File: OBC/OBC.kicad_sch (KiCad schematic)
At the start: 10 parts, among them J101 IDC1 (PMS-Raspi), J102 Modo de operación, J103 IDC2 (Raspi-TRU), J104 Conn_01x04, U101 RASPBERRY_PI_ZERO_2_W, U102 BMP280, U103 MPU9250

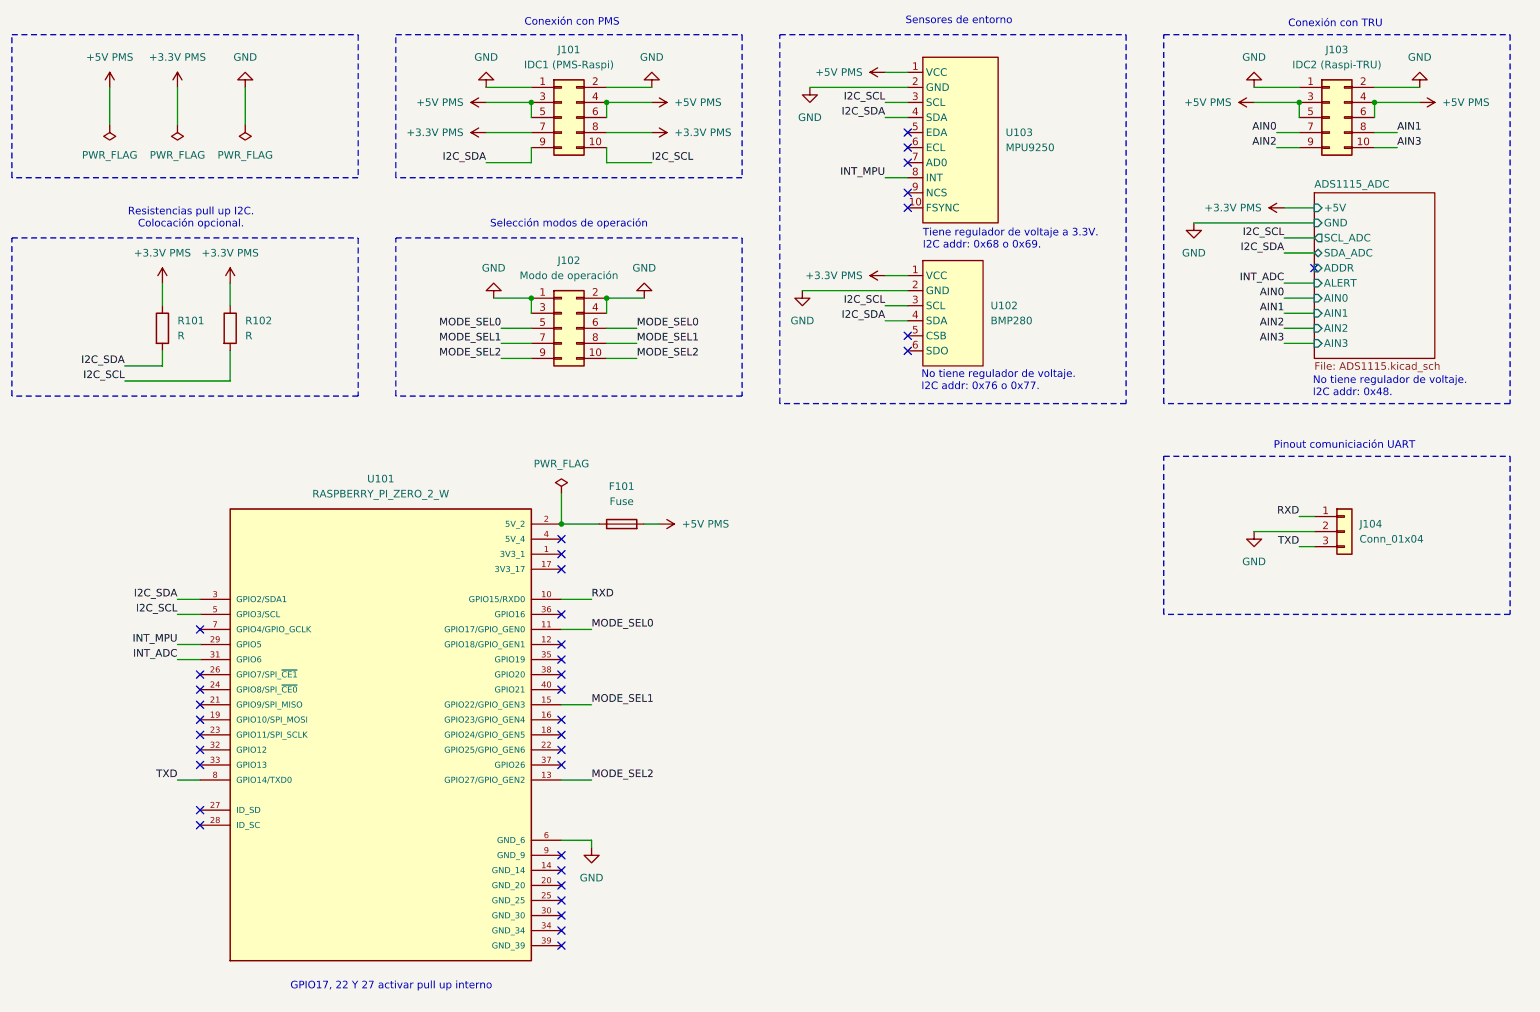
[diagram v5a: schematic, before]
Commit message: Cambia conectores IDC por JST
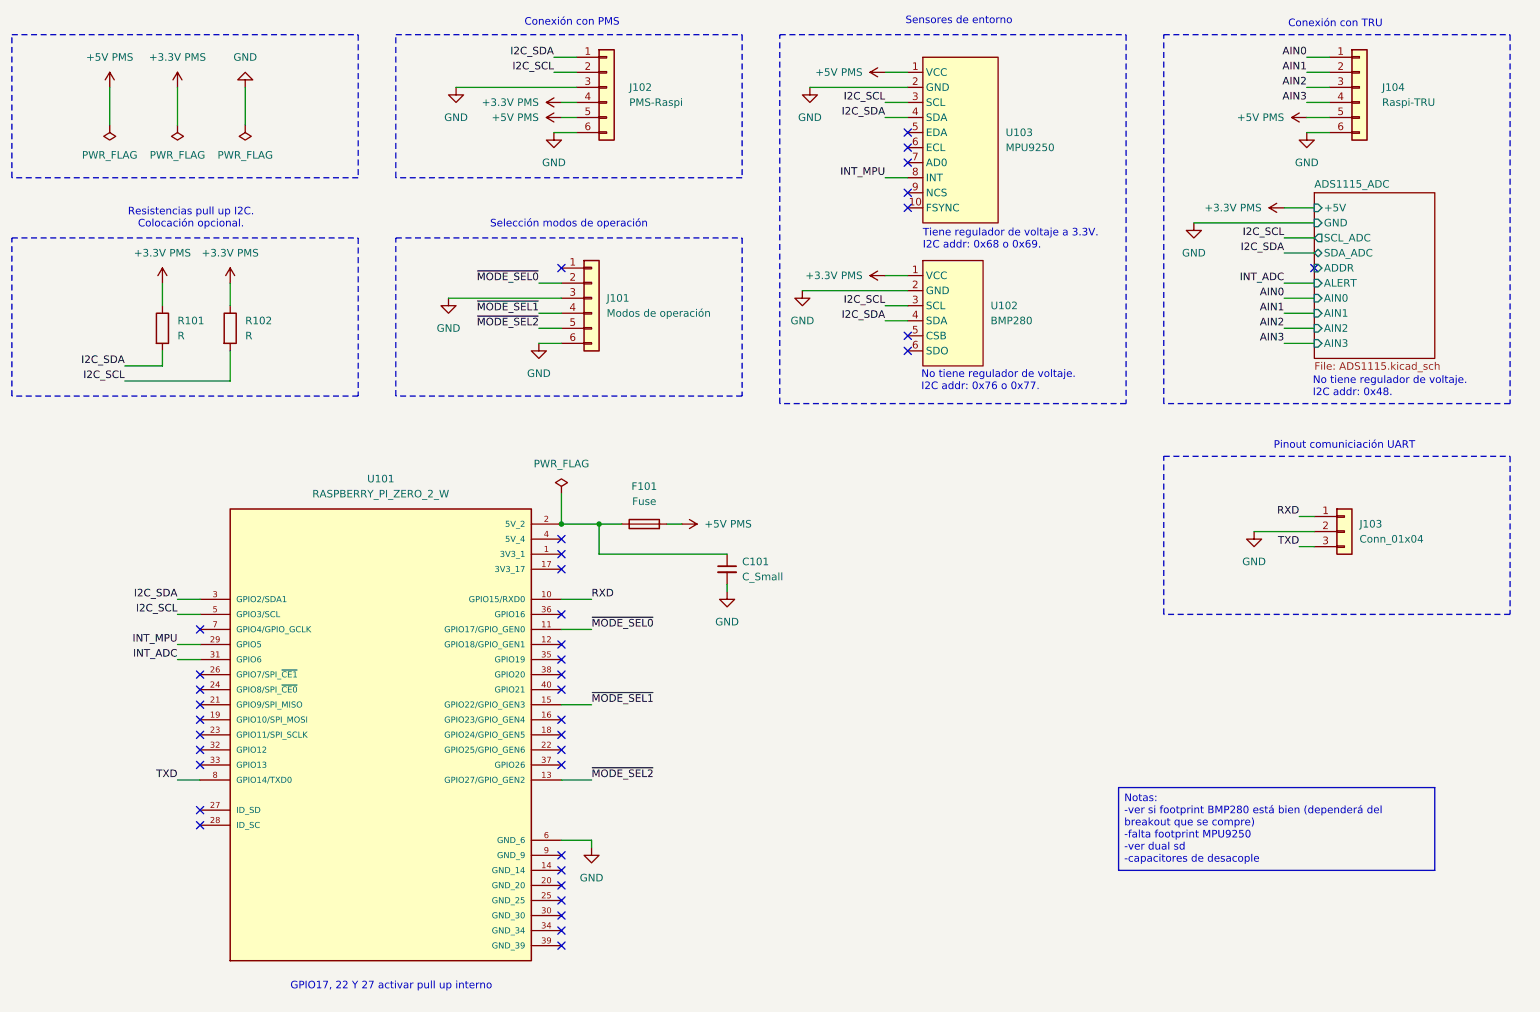
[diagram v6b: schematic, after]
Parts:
- removed J101: IDC1 (PMS-Raspi), symbol Connector_Generic:Conn_02x05_Odd_Even
- removed J102: Modo de operación, symbol Connector_Generic:Conn_02x05_Odd_Even
- removed J103: IDC2 (Raspi-TRU), symbol Connector_Generic:Conn_02x05_Odd_Even
- added C101: C_Small, symbol Device:C_Small
- added J101: Modos de operación, symbol Connector_Generic:Conn_01x06
- added J102: PMS-Raspi, symbol Connector_Generic:Conn_01x06
- added J104: Raspi-TRU, symbol Connector_Generic:Conn_01x06
- renumbered J104 to J103
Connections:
- net +3.3V PMS: now also J102.4 (Pin_4)
- net +5V PMS: now also J102.5 (Pin_5), J104.5 (Pin_5)
- net AIN0: now also J104.1 (Pin_1)
- net AIN1: now also J104.2 (Pin_2)
- net AIN2: now also J104.3 (Pin_3)
- net AIN3: now also J104.4 (Pin_4)
- net GND: now also C101.2, J101.3 (Pin_3), J101.6 (Pin_6), J102.3 (Pin_3), J102.6 (Pin_6), J104.6 (Pin_6)
- net I2C_SCL: now also J102.2 (Pin_2)
- net I2C_SDA: now also J102.1 (Pin_1)
- net at F101.1, U101.2 (5V_2): now also C101.1
- net MODE_SEL0 renamed ~{MODE_SEL0}
- net ~{MODE_SEL0}: now also J101.2 (Pin_2)
- net MODE_SEL1 renamed ~{MODE_SEL1}
- net ~{MODE_SEL1}: now also J101.4 (Pin_4)
- net MODE_SEL2 renamed ~{MODE_SEL2}
- net ~{MODE_SEL2}: now also J101.5 (Pin_5)
- no-connect marks 37 -> 38
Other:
- moved on the sheet: F101

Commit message: Agrega resistencias en serie con NTC
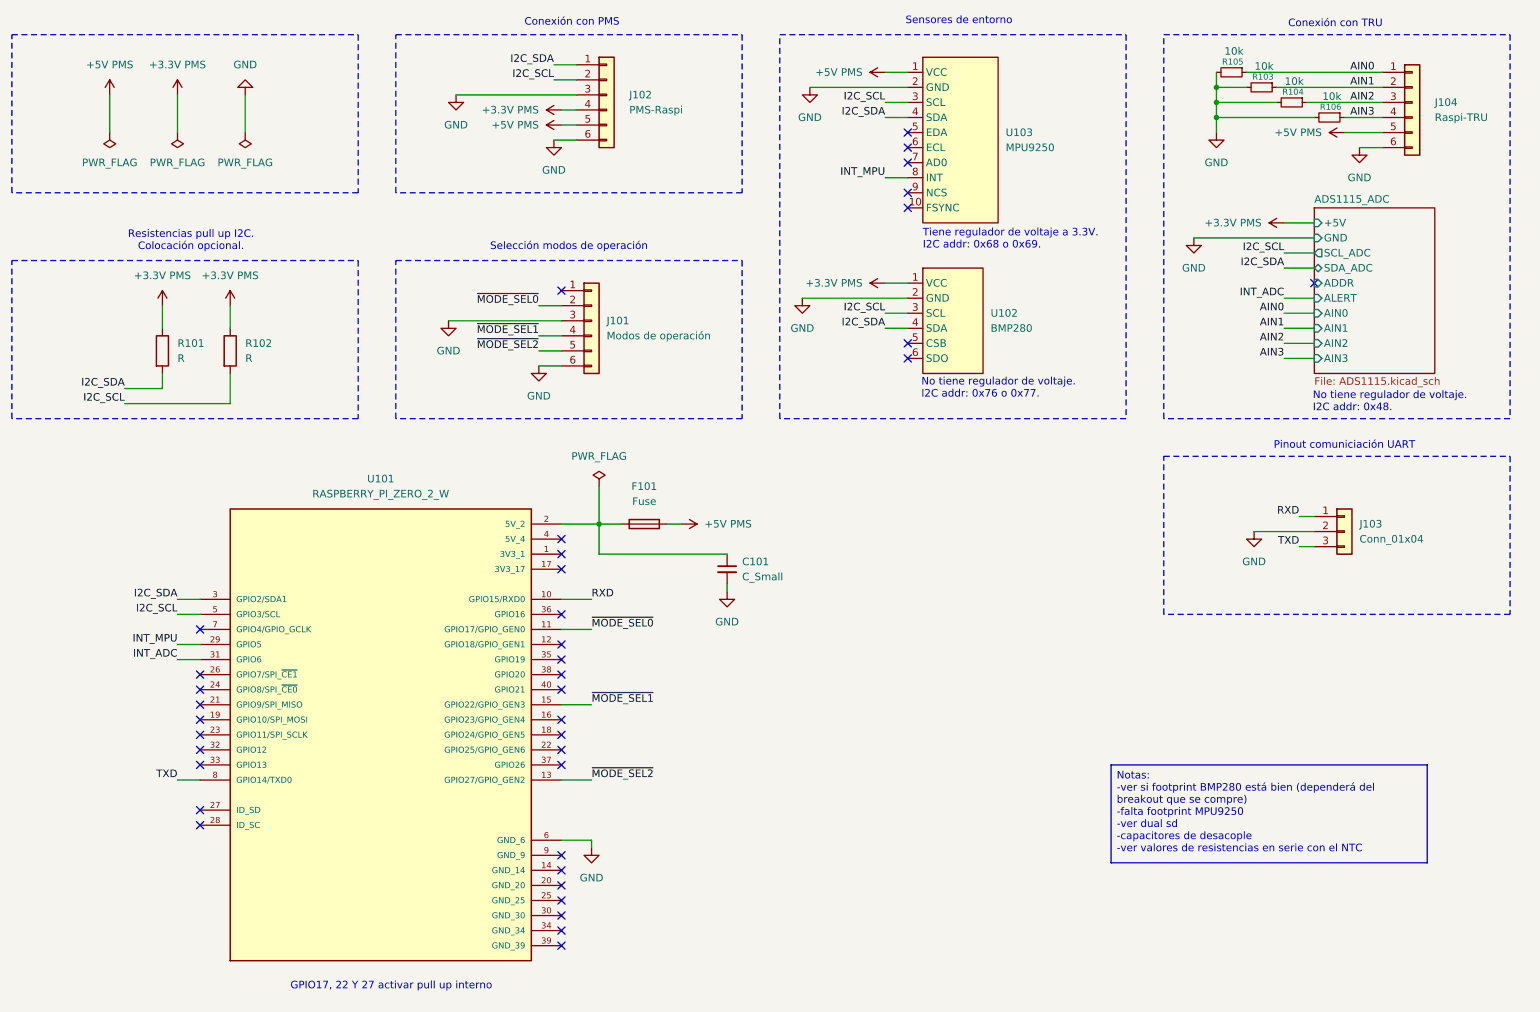
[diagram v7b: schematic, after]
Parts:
- added R103, R104, R105, R106: 10k, symbol Device:R_Small
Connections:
- net AIN0: now also R105.1
- net AIN1: now also R103.1
- net AIN2: now also R104.1
- net AIN3: now also R106.1
- net GND: now also R103.2, R104.2, R105.2, R106.2
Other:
- moved on the sheet: J101, J102, J104, R101, R102, U102

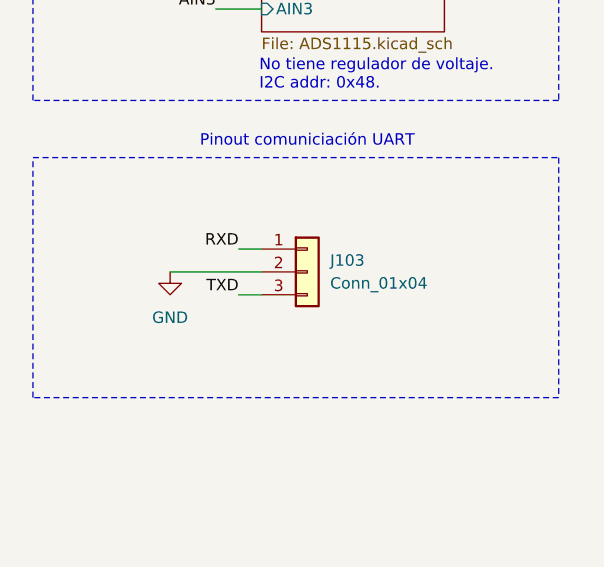
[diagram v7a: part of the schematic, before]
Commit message: Empieza con pcb
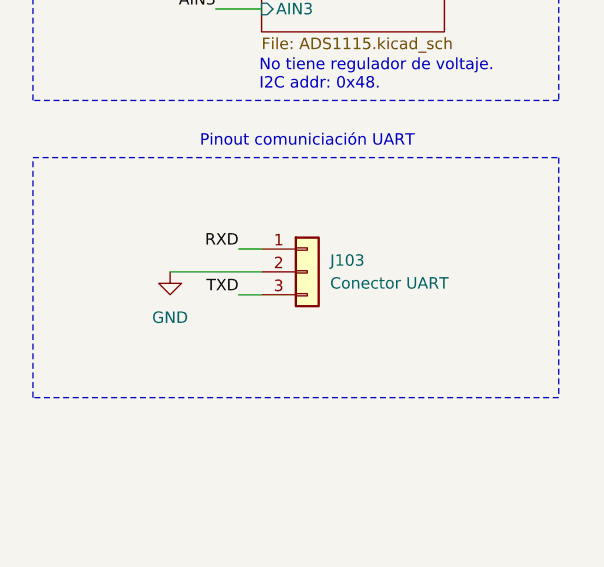
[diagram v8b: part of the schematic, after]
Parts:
- C101: footprint (none) -> Capacitor_SMD:C_0402_1005Metric
- F101: footprint (none) -> Fuse:Fuse_BelFuse_0ZRE0005FF_L8.3mm_W3.8mm
- J101, J102, J104: footprint (none) -> Connector_JST:JST_XH_S6B-XH-A_1x06_P2.50mm_Horizontal
- J103: value Conn_01x04 -> Conector UART; footprint (none) -> Connector_JST:JST_XH_S3B-XH-A-1_1x03_P2.50mm_Horizontal
- R101, R102, R103, R104, R105, R106: footprint (none) -> Resistor_SMD:R_0603_1608Metric
- U102: footprint Charleslabs_Parts:BMP280_Module -> cubesat:BMP280_Module
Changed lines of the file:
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@@
 			)
 		)
-		(property "Footprint" ""
+		(property "Footprint" "Resistor_SMD:R_0603_1608Metric"
 			(at 242.57 38.1 0)
 			(effects
@@
 			)
 		)
-		(property "Footprint" ""
+		(property "Footprint" "Connector_JST:JST_XH_S6B-XH-A_1x06_P2.50mm_Horizontal"
 			(at 120.65 34.29 0)
 			(effects
@@
 			)
 		)
-		(property "Footprint" ""
+		(property "Footprint" "Connector_JST:JST_XH_S6B-XH-A_1x06_P2.50mm_Horizontal"
 			(at 256.54 35.56 0)
 			(effects
@@
 			)
 		)
-		(property "Footprint" ""
+		(property "Footprint" "Capacitor_SMD:C_0402_1005Metric"
 			(at 140.97 114.3 0)
 			(effects
@@
 			)
 		)
-		(property "Footprint" ""
+		(property "Footprint" "Resistor_SMD:R_0603_1608Metric"
 			(at 236.22 35.56 0)
 			(effects
@@
 			)
 		)
-		(property "Footprint" ""
+		(property "Footprint" "Resistor_SMD:R_0603_1608Metric"
 			(at 55.372 77.47 90)
 			(effects
@@
 			)
 		)
-		(property "Footprint" ""
+		(property "Footprint" "Connector_JST:JST_XH_S6B-XH-A_1x06_P2.50mm_Horizontal"
 			(at 118.11 72.39 0)
 			(effects
@@
 			)
 		)
-		(property "Footprint" "Charleslabs_Parts:BMP280_Module"
+		(property "Footprint" "cubesat:BMP280_Module"
 			(at 179.07 72.39 0)
 			(effects
@@
 			)
 		)
-		(property "Footprint" ""
+		(property "Footprint" "Resistor_SMD:R_0603_1608Metric"
 			(at 226.06 30.48 0)
 			(effects
@@
 			)
 		)
-		(property "Footprint" ""
+		(property "Footprint" "Fuse:Fuse_BelFuse_0ZRE0005FF_L8.3mm_W3.8mm"
 			(at 127 108.458 90)
 			(effects
@@
 			)
 		)
-		(property "Footprint" ""
+		(property "Footprint" "Resistor_SMD:R_0603_1608Metric"
 			(at 43.942 77.47 90)
 			(effects
@@
 			)
 		)
-		(property "Value" "Conn_01x04"
+		(property "Value" "Conector UART"
 			(at 247.65 109.2199 0)
 			(effects
@@
 			)
 		)
-		(property "Footprint" ""
+		(property "Footprint" "Connector_JST:JST_XH_S3B-XH-A-1_1x03_P2.50mm_Horizontal"
 			(at 245.11 107.95 0)
 			(effects
@@
 			)
 		)
-		(property "Footprint" ""
+		(property "Footprint" "Resistor_SMD:R_0603_1608Metric"
 			(at 231.14 33.02 0)
 			(effects
